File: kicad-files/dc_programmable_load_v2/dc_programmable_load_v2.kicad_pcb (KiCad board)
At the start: 2 copper layers, 95 x 79.5 mm, 43 parts, among them J1 DC Jack 12V, J3 Conn_01x04_Socket, Q1 IRF3205, U1 LM358DR, U2 ER_OLEDM0.91_1x-I2C, U3 AP63200WU, U4 DS18B20

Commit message: Update v2 PCB layout and project settings
Co-Authored-By: Claude Opus 4.8 (1M context) <noreply@anthropic.com>
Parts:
- moved L1 32.9 mm to (174.5, 78.5)
- moved R12 27.7 mm to (183.5, 96.5), turned to 0 degrees
- moved R11 25.8 mm to (183.5, 84.0), turned to 0 degrees
- moved C14 7.83 mm to (171.0, 86.3)
- moved C15 7.83 mm to (174.5, 86.3)
- moved R10 7.83 mm to (181.0, 93.0)
- moved R9 7.83 mm to (181.0, 88.0)
- moved S1 7.83 mm to (195.0, 90.5)
- moved C9 2.64 mm to (191.8, 105.8), turned to -90 degrees
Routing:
- net Net-(U3-SW): track 58.6 -> 20.1 mm
- net /netbot1: track 31.3 -> 63.4 mm
- net /nettop1: track 76.4 -> 53.1 mm, vias 2 -> 0
- net /12V: track 119.8 -> 100.9 mm
- net Net-(R11-Pad2): track 2.68 -> 19.2 mm
- net Net-(R12-Pad2): track 2.68 -> 19.0 mm
- net GND: vias 247 -> 262
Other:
- board size 95 x 79.5 mm -> 85.2 x 79.5 mm

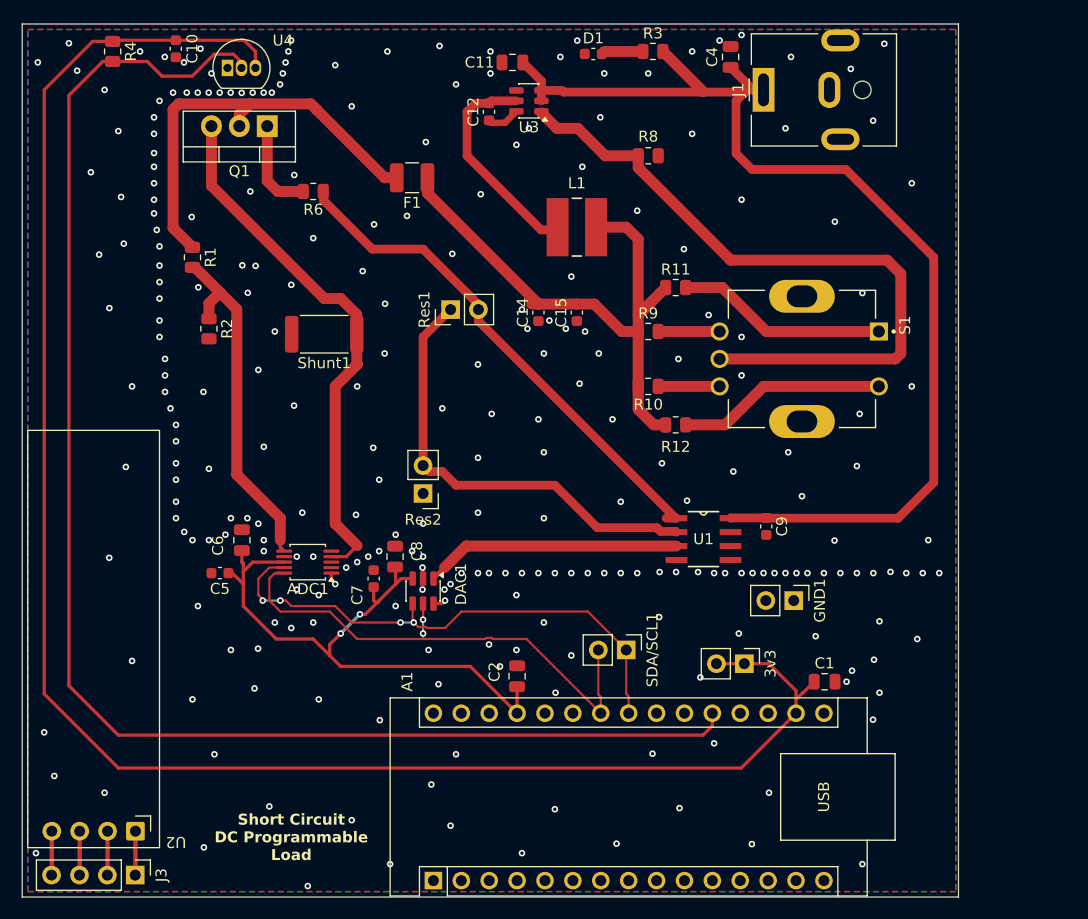
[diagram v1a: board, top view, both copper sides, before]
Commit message: Update v2 schematic and PCB layout
Co-Authored-By: Claude Opus 5 (1M context) <noreply@anthropic.com>
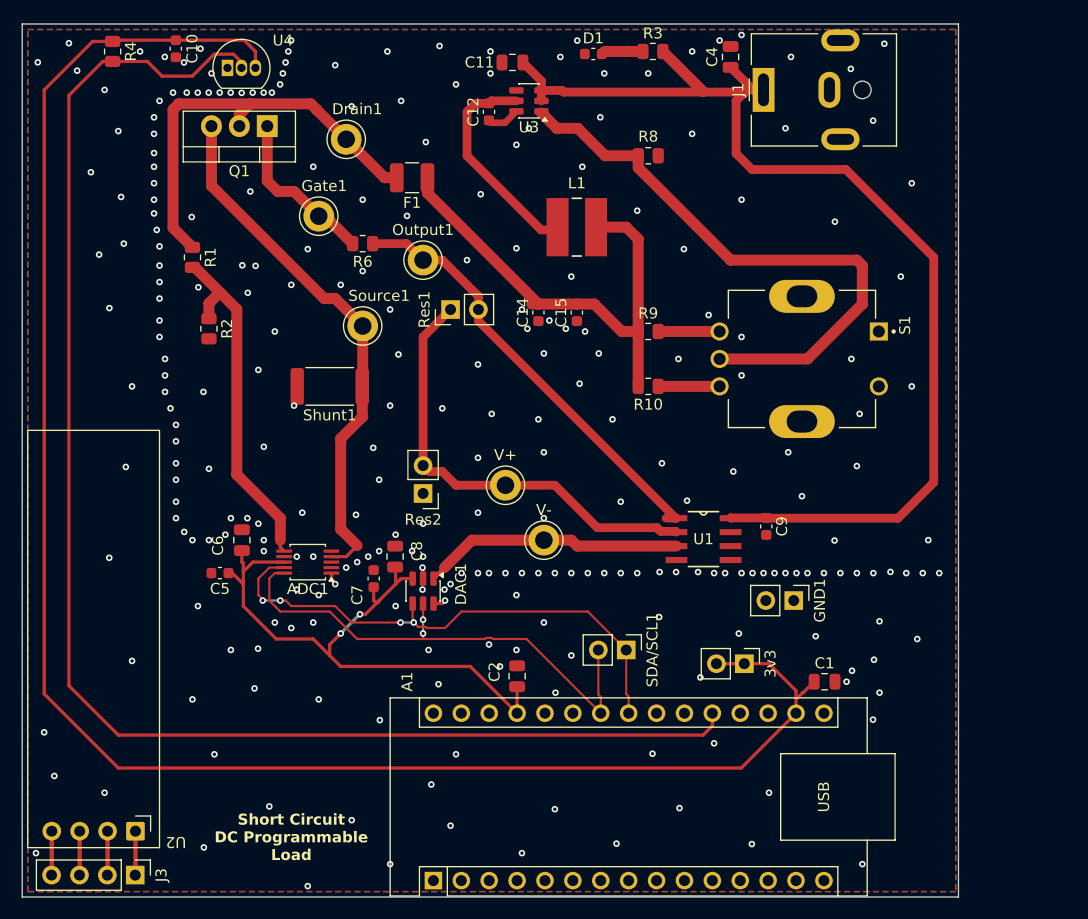
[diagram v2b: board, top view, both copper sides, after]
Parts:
- removed R11: 4.7k, Resistor_SMD:R_0805_2012Metric
- removed R12: 3.3k, Resistor_SMD:R_0805_2012Metric
- added Drain1: TestPoint, TestPoint:TestPoint_Keystone_5010-5014_Multipurpose, F.Cu at (153.5, 70.5)
- added Gate1: TestPoint, TestPoint:TestPoint_Keystone_5010-5014_Multipurpose, F.Cu at (151.0, 77.5)
- added Output1: TestPoint, TestPoint:TestPoint_Keystone_5010-5014_Multipurpose, F.Cu at (160.5, 81.5)
- added Source1: TestPoint, TestPoint:TestPoint_Keystone_5010-5014_Multipurpose, F.Cu at (155.0, 87.5)
- added V+: TestPoint, TestPoint:TestPoint_Keystone_5010-5014_Multipurpose, F.Cu at (168.0, 102.0)
- added V-: TestPoint, TestPoint:TestPoint_Keystone_5010-5014_Multipurpose, F.Cu at (171.5, 107.0)
- R10: value 1k -> 77.5k
- R9: value 2.2k -> 52.5k
- moved R6 6.54 mm to (155.0, 80.0)
- moved Shunt1 4.78 mm to (152.0, 93.0)
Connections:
- S1 pad 1: Net-(R11-Pad2) -> unconnected-(S1-Pad1)
- S1 pad 2: Net-(R12-Pad2) -> unconnected-(S1-Pad2)
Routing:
- net Net-(R11-Pad2): track 19.2 -> 0.00 mm
- net Net-(R12-Pad2): track 19.0 -> 0.00 mm
- net /netbot1: track 63.4 -> 54.2 mm
- net /nettop1: track 53.1 -> 44.1 mm
- net /opamp_output: track 46.8 -> 40.3 mm
- net Net-(Q1-G): track 8.67 -> 15.1 mm
- net GND: vias 262 -> 266
